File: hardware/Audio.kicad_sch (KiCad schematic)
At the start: 84 parts, among them IC1 LM4861M, J1 Kenwood-2.5, J11 Radio_Opt, J12 Speaker, J4 CAT_TX, J5 Kenwood-3.5, J6 CAT_TX, J7 Radio, Q1 IRLML2060, Q2 BSS138, Q3 BSS138, U1 MAX9814, U6 MCP6002, U7 MCP6002

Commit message: Updated schematic title block
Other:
- company: (none) -> M17Project
- title: (none) -> Module17
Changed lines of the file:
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@@
 (kicad_sch (version 20230121) (generator eeschema)
   (paper "A4")
+  (title_block
+    (title "Module17")
+    (date "2023-07-18")
+    (rev "Rev 1.0")
+    (company "M17Project")
+    (comment 1 "Mathis - DB9MAT")
+    (comment 2 "Wojciech - SP5WWP")
+    (comment 3 "Authors:")
+  )
   (junction (at 129.54 151.13) (diameter 0) (color 0 0 0 0)
   )

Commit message: Deleted unused parts fields
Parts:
- IC1: Manufacturer_Name Texas Instruments -> (none); Mouser Part Number 926-LM4861MX/NOPB -> (none); Mouser Price/Stock https://www.mouser.co.uk/ProductDetail/Texas-Instruments/LM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 -> (none)
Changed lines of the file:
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@@
-      (effects (font (size 1.27 1.27)) hide)
-    )
-    (property "PartNo" "" (at 163.83 118.11 0)
       (effects (font (size 1.27 1.27)) hide)
     )
@@
       (effects (font (size 1.27 1.27)) (justify left) hide)
     )
-    (property "Mouser Part Number" "926-LM4861MX/NOPB" (at 106.68 46.99 0)
-      (effects (font (size 1.27 1.27)) (justify left) hide)
-    )
-    (property "Mouser Price/Stock" "https://www.mouser.co.uk/ProductDetail/Texas-Instruments/LM4861MX-NOPB?qs=QbsRYf82W3FxTp8pKIvxnw%3D%3D" (at 106.68 49.53 0)
-      (effects (font (size 1.27 1.27)) (justify left) hide)
-    )
-    (property "Manufacturer_Name" "Texas Instruments" (at 106.68 52.07 0)
-      (effects (font (size 1.27 1.27)) (justify left) hide)
-    )
     (property "MPN" "LM4861MX/NOPB" (at 77.47 39.37 0)
       (effects (font (size 1.27 1.27)) hide)
@@
       (effects (font (size 1.27 1.27)) hide)
     )
-    (property "PartNo" "" (at 229.87 44.45 0)
-      (effects (font (size 1.27 1.27)) hide)
-    )

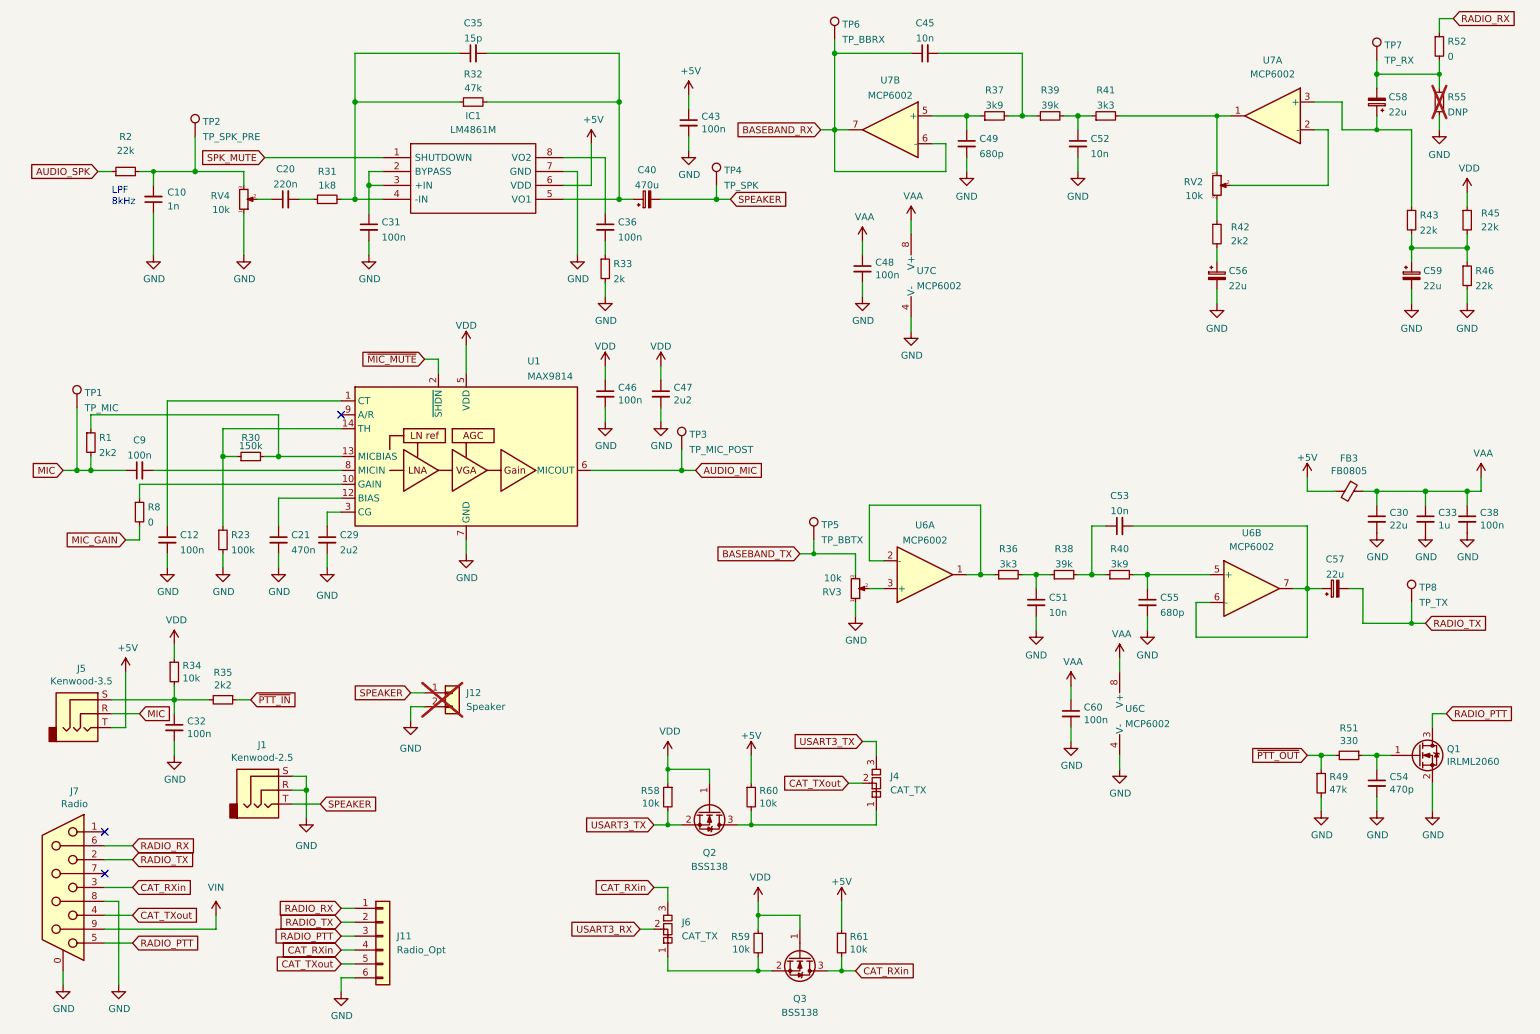
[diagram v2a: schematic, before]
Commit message: Added OHIS connector to the schematic
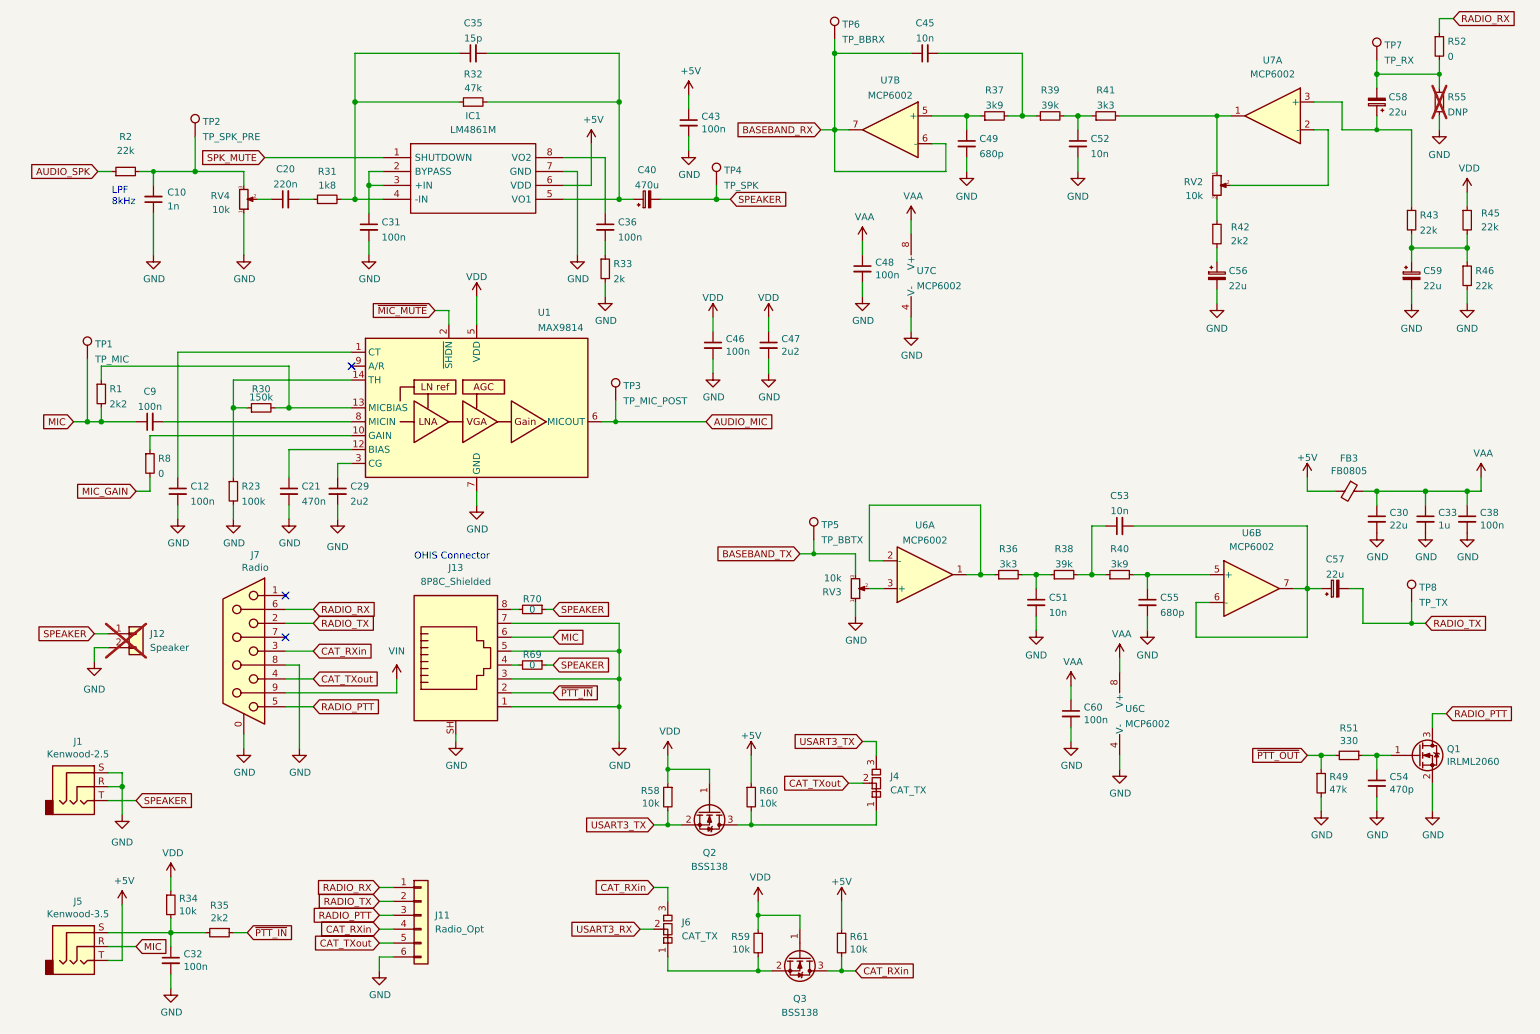
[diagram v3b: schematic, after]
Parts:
- added J13: 8P8C_Shielded, symbol Connector:8P8C_Shielded
- added R69, R70: 0, pkl_dipol:R_0603, symbol pkl_device:pkl_R_Small
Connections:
- net GND: now also J13.1, J13.3, J13.5, J13.7, J13.SH
- net MIC: now also J13.6
- net SPEAKER: now also R69.1, R70.1
- net ~{PTT_IN}: now also J13.2
- new net: J13.4, R69.2
- new net: J13.8, R70.2
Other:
- note added: "OHIS Connector"
- moved on the sheet: C12, C21, C29, C32, C46, C47, C9, J1, J11, J12, J5, J7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

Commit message: Reworked audio output diagram
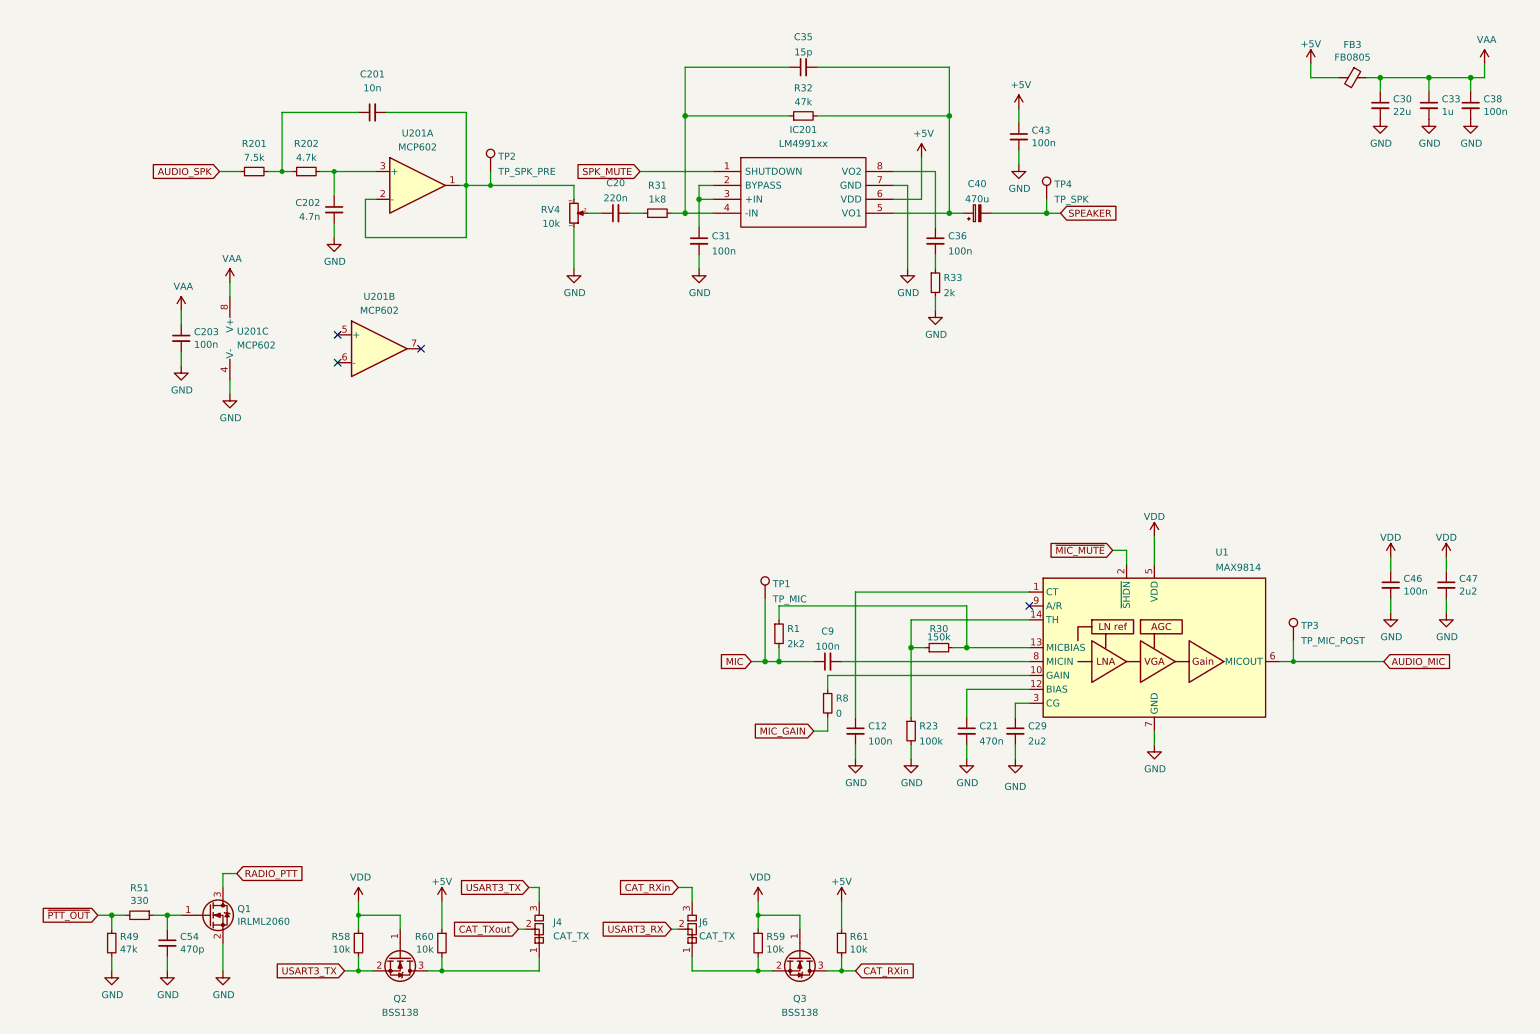
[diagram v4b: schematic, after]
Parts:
- removed C10: 1n, pkl_dipol:C_0603, symbol pkl_device:pkl_C_Small
- removed C32, C48, C60: 100n, pkl_dipol:C_0603, symbol pkl_device:pkl_C_Small
- removed C45, C51, C52, C53: 10n, pkl_dipol:C_0603, symbol pkl_device:pkl_C_Small
- removed C49, C55: 680p, pkl_dipol:C_0603, symbol pkl_device:pkl_C_Small
- removed C56, C57, C58, C59: 22u, Capacitor_Tantalum_SMD:CP_EIA-3216-18_Kemet-A, symbol pkl_device:pkl_CP_Small
- removed IC1: LM4861M, Package_SO:SOIC-8_3.9x4.9mm_P1.27mm, symbol Module17:LM4861MX_NOPB
- removed J1: Kenwood-2.5, M17-SmartMic:PJ-211A, symbol Connector:AudioJack3
- removed J11: Radio_Opt, Connector_PinHeader_2.54mm:PinHeader_1x06_P2.54mm_Vertical, symbol Connector_Generic:Conn_01x06
- removed J12: Speaker, Connector_PinHeader_2.54mm:PinHeader_1x02_P2.54mm_Vertical, symbol Connector_Generic:Conn_01x02
- removed J13: 8P8C_Shielded, symbol Connector:8P8C_Shielded
- removed J5: Kenwood-3.5, M17-SmartMic:PJ-3136-B, symbol Connector:AudioJack3
- removed J7: Radio, Connector_Dsub:DSUB-9_Female_Horizontal_P2.77x2.84mm_EdgePinOffset4.94mm_Housed_MountingHolesOffset7.48mm, symbol Connector:DB9_Female_MountingHoles
- removed R2, R43, R45, R46: 22k, pkl_dipol:R_0603, symbol pkl_device:pkl_R_Small
- removed R34: 10k, pkl_dipol:R_0603, symbol pkl_device:pkl_R_Small
- removed R35, R42: 2k2, pkl_dipol:R_0603, symbol pkl_device:pkl_R_Small
- removed R36, R41: 3k3, pkl_dipol:R_0603, symbol pkl_device:pkl_R_Small
- removed R37, R40: 3k9, pkl_dipol:R_0603, symbol pkl_device:pkl_R_Small
- removed R38, R39: 39k, pkl_dipol:R_0603, symbol pkl_device:pkl_R_Small
- removed R52, R69, R70: 0, pkl_dipol:R_0603, symbol pkl_device:pkl_R_Small
- removed R55: DNP, pkl_dipol:R_0603, symbol pkl_device:pkl_R_Small
- removed RV2, RV3: 10k, Potentiometer_SMD:Potentiometer_Bourns_3224W_Vertical, symbol Device:R_Potentiometer_Small
- removed TP5: TP_BBTX, TestPoint:TestPoint_Pad_D1.0mm, symbol Connector:TestPoint
- removed TP6: TP_BBRX, TestPoint:TestPoint_Pad_D1.0mm, symbol Connector:TestPoint
- removed TP7: TP_RX, TestPoint:TestPoint_Pad_D1.0mm, symbol Connector:TestPoint
- removed TP8: TP_TX, TestPoint:TestPoint_Pad_D1.0mm, symbol Connector:TestPoint
- removed U6, U7: MCP6002, Package_SO:SOIC-8_3.9x4.9mm_P1.27mm, symbol Amplifier_Operational:MCP602
- added C201: 10n, symbol Device:C_Small
- added C202: 4.7n, symbol Device:C_Small
- added C203: 100n, pkl_dipol:C_0603, symbol pkl_device:pkl_C_Small
- added IC201: LM4991xx, SOIC127P600X175-8N, symbol Module17:LM4991xx
- added R201: 7.5k, symbol Device:R_Small
- added R202: 4.7k, symbol Device:R_Small
- added U201: MCP602, symbol Amplifier_Operational:MCP602
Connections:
- net +5V: now also IC201.6 (VDD)
- net AUDIO_SPK: now also R201.1
- net GND: now also C202.2, C203.2, IC201.7 (GND), U201.4 (V-)
- net SPK_MUTE: now also IC201.1 (SHUTDOWN)
- net VAA: now also C203.1, U201.8 (V+)
- net at RV4.3, TP2.1: now also C201.2, U201.1, U201.2 (-)
- net at C35.1, R31.2, R32.1: now also IC201.4 (-IN)
- net at C36.1: now also IC201.8 (VO2)
- net at C35.2, C40.1, R32.2: now also IC201.5 (VO1)
- net at C31.1: now also IC201.2 (BYPASS), IC201.3 (+IN)
- new net: C202.1, R202.2, U201.3 (+)
- new net: C201.1, R201.2, R202.1
- no-connect marks 3 -> 4
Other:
- note removed: "LPF 8kHz"
- note removed: "OHIS Connector"
- moved on the sheet: C12, C20, C21, C29, C30, C31, C33, C35, C36, C38, C40, C43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

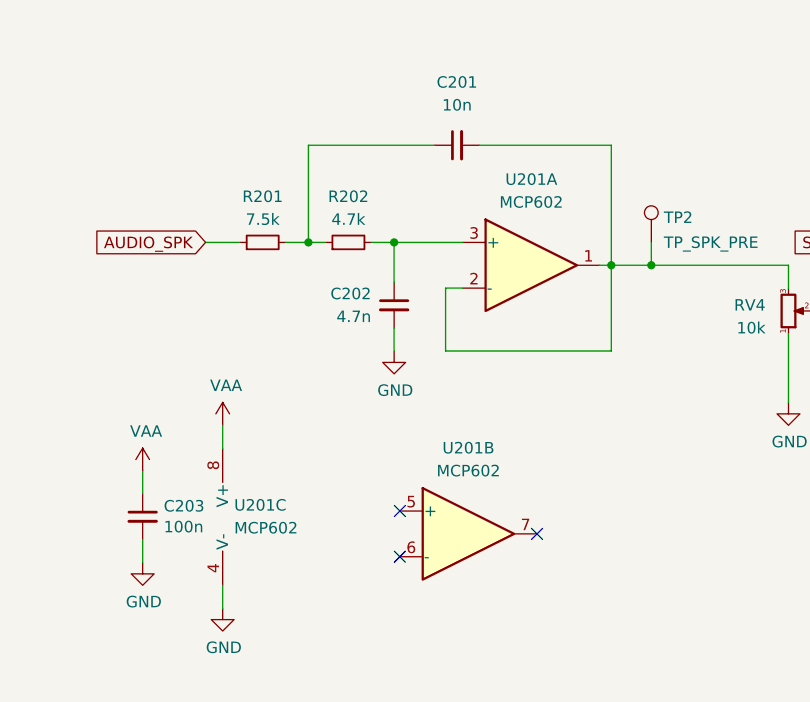
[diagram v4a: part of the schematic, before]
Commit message: Assigned footprints
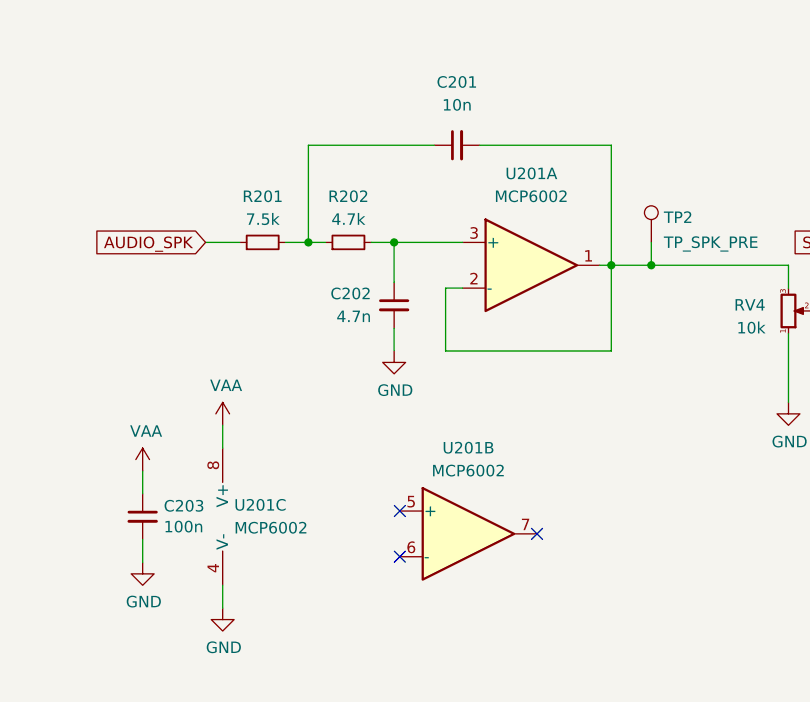
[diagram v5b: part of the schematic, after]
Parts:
- C201, C202: footprint (none) -> pkl_dipol:C_0603
- IC201: footprint SOIC127P600X175-8N -> Package_SO:SOIC-8_3.9x4.9mm_P1.27mm
- R201, R202: footprint (none) -> pkl_dipol:R_0603
- U201: value MCP602 -> MCP6002; footprint (none) -> Package_SO:SOIC-8_3.9x4.9mm_P1.27mm
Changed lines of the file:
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@@
   (symbol (lib_id "Amplifier_Operational:MCP602") (at 83.82 44.45 0) (unit 1)
     (in_bom yes) (on_board yes) (dnp no) (fields_autoplaced)
-    (property "Reference" "U201" (at 83.82 34.925 0)
-      (effects (font (size 1.27 1.27)))
-    )
-    (property "Value" "MCP602" (at 83.82 37.465 0)
-      (effects (font (size 1.27 1.27)))
-    )
-    (property "Footprint" "" (at 83.82 44.45 0)
+    (property "Reference" "U201" (at 83.82 34.29 0)
+      (effects (font (size 1.27 1.27)))
+    )
+    (property "Value" "MCP6002" (at 83.82 36.83 0)
+      (effects (font (size 1.27 1.27)))
+    )
+    (property "Footprint" "Package_SO:SOIC-8_3.9x4.9mm_P1.27mm" (at 83.82 44.45 0)
       (effects (font (size 1.27 1.27)) hide)
     )
@@
       (effects (font (size 1.27 1.27)))
     )
-    (property "Footprint" "" (at 75.565 31.115 0)
+    (property "Footprint" "pkl_dipol:C_0603" (at 75.565 31.115 0)
       (effects (font (size 1.27 1.27)) hide)
     )
@@
       (effects (font (size 1.27 1.27)))
     )
-    (property "Footprint" "" (at 63.5 41.91 0)
+    (property "Footprint" "pkl_dipol:R_0603" (at 63.5 41.91 0)
       (effects (font (size 1.27 1.27)) hide)
     )
@@
       (effects (font (size 1.27 1.27)))
     )
-    (property "Footprint" "SOIC127P600X175-8N" (at 167.005 39.37 0)
+    (property "Footprint" "Package_SO:SOIC-8_3.9x4.9mm_P1.27mm" (at 167.005 39.37 0)
       (effects (font (size 1.27 1.27)) (justify left) hide)
     )
@@
       (effects (font (size 1.27 1.27)))
     )
-    (property "Footprint" "" (at 53.975 41.91 0)
+    (property "Footprint" "pkl_dipol:R_0603" (at 53.975 41.91 0)
       (effects (font (size 1.27 1.27)) hide)
     )
@@
       (effects (font (size 1.27 1.27)))
     )
-    (property "Value" "MCP602" (at 76.835 67.31 0)
-      (effects (font (size 1.27 1.27)))
-    )
-    (property "Footprint" "" (at 76.835 74.295 0)
+    (property "Value" "MCP6002" (at 76.835 67.31 0)
+      (effects (font (size 1.27 1.27)))
+    )
+    (property "Footprint" "Package_SO:SOIC-8_3.9x4.9mm_P1.27mm" (at 76.835 74.295 0)
       (effects (font (size 1.27 1.27)) hide)
     )
@@
       (effects (font (size 1.27 1.27)) (justify left))
     )
-    (property "Footprint" "" (at 68.58 48.895 0)
+    (property "Footprint" "pkl_dipol:C_0603" (at 68.58 48.895 0)
       (effects (font (size 1.27 1.27)) hide)
     )
@@
       (effects (font (size 1.27 1.27)) (justify left))
     )
-    (property "Value" "MCP602" (at 50.8 73.66 0)
-      (effects (font (size 1.27 1.27)) (justify left))
-    )
-    (property "Footprint" "" (at 52.07 72.39 0)
-      (effects (font (size 1.27 1.27)) hide)
-    )
+    (property "Value" "MCP6002" (at 50.8 73.66 0)
+      (effects (font (size 1.27 1.27)) (justify left))
+    )
+    (property "Footprint" "Package_SO:SOIC-8_3.9x4.9mm_P1.27mm" (at 52.07 72.39 0)
+      (effects (font (size 1.27 1.27)) hide)
+    )

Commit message: Modified components references
Modified references to fit the previous references (from before adding the new sheets)
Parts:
- renumbered IC201 to IC1
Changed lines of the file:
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@@
   (symbol (lib_id "Module17:LM4991xx") (at 137.795 41.91 0) (unit 1)
     (in_bom yes) (on_board yes) (dnp no) (fields_autoplaced)
-    (property "Reference" "IC201" (at 154.305 34.29 0)
+    (property "Reference" "IC1" (at 154.305 34.29 0)
       (effects (font (size 1.27 1.27)))
     )
@@
       (project "M17-SmartMic"
         (path "/59592280-3207-432b-a891-cd517ec5cf12/00000000-0000-0000-0000-0000612c969e"
-          (reference "IC201") (unit 1)
+          (reference "IC1") (unit 1)
         )
       )

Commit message: Switched to M17_kicad_library for custom symbols/footprints
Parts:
- removed IC1: LM4991xx, Package_SO:SOIC-8_3.9x4.9mm_P1.27mm, symbol Module17:LM4991xx
- added IC1: LM4991xx, Package_SO:SOIC-8_3.9x4.9mm_P1.27mm, symbol M17_audio:LM4991xx
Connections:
- net +5V: now also IC1.6 (VDD)
- net GND: now also IC1.7 (GND)
- net SPK_MUTE: now also IC1.1 (SHUTDOWN)
- net at C35.1, R31.2, R32.1: now also IC1.4 (-IN)
- net at C36.1: now also IC1.8 (VO2)
- net at C35.2, C40.1, R32.2: now also IC1.5 (VO1)
- net at C31.1: now also IC1.2 (BYPASS), IC1.3 (+IN)
